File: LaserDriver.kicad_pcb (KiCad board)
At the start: 2 copper layers, 21 parts, among them J100 Screw_Terminal_01x02, J101 Screw_Terminal_01x02, J102 Screw_Terminal_01x02, U1 TPS92513DGQR

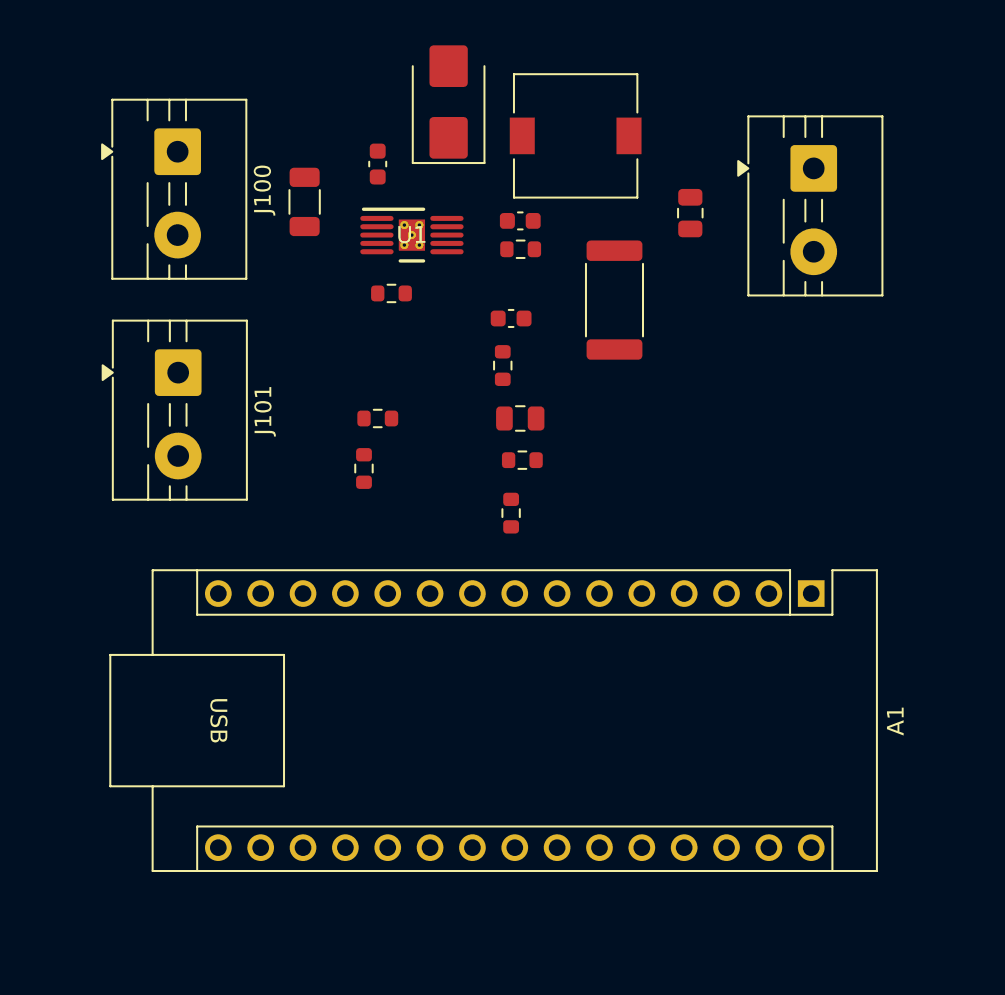
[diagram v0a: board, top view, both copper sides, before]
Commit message: add arduino 3d model
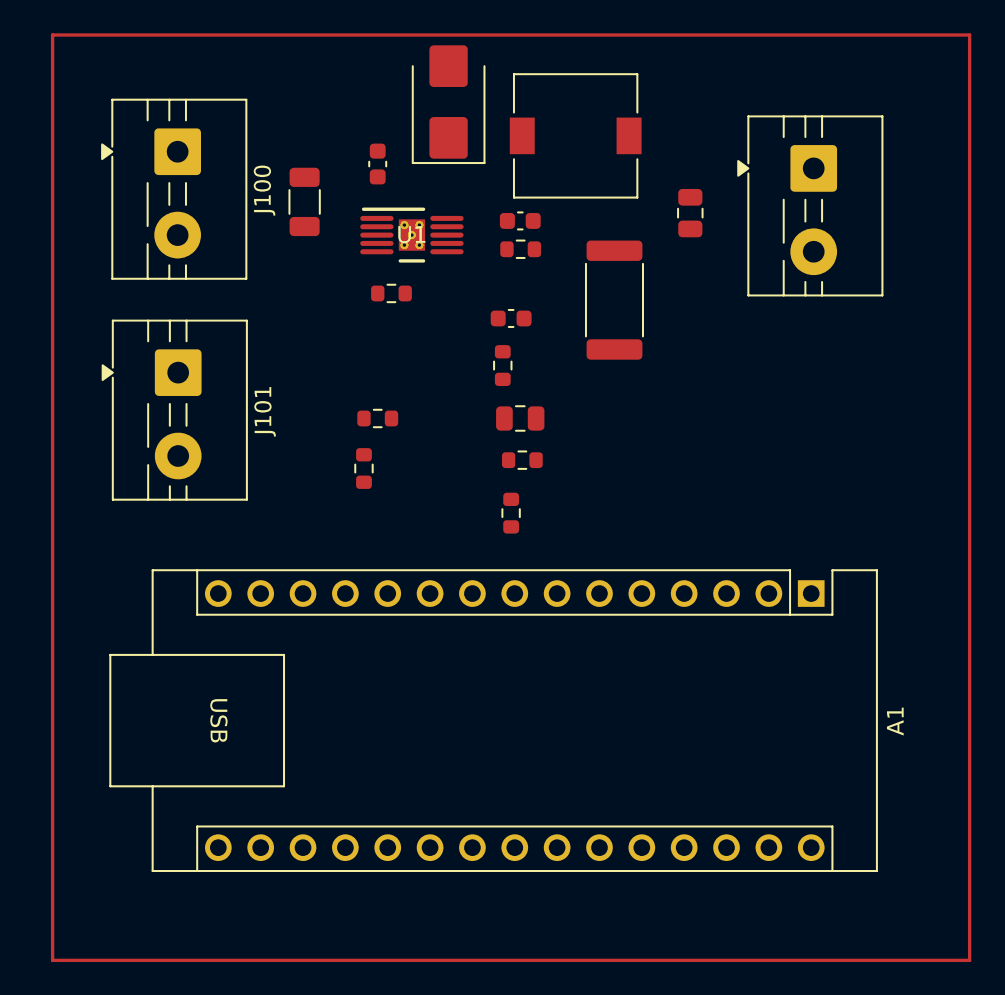
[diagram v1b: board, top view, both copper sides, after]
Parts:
- A1: footprint Module:Arduino_Nano -> Arduino:Arduino_Nano
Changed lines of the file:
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@@
 		)
 	)
-	(footprint "Module:Arduino_Nano"
+	(footprint "Arduino:Arduino_Nano"
 		(layer "F.Cu")
 		(at 69.5 119.5 -90)
@@
 		(tags "Arduino Nano")
 		(property "Reference" "A1"
-			(at 7.62 -5.08 90)
+			(at 7.62 -5.08 270)
 			(layer "F.SilkS")
 			(effects
@@
 			)
 			(scale
+				(xyz 2 1 1)
+			)
+			(rotate
+				(xyz -0 -0 -0)
+			)
+		)
+		(model "${KICAD9_FOOTPRINT_DIR}/Connector_PinSocket_2.54mm.pretty/PinSocket_1x15_P2.54mm_Horizontal.kicad_mod"
+			(offset
+				(xyz 0 0 0)
+			)
+			(scale
+				(xyz 1 1 1)
+			)
+			(rotate
+				(xyz -0 -0 -0)
+			)
+		)
+		(model "${KICAD9_3DMODEL_DIR}/Connector_PinSocket_2.54mm.3dshapes/PinSocket_1x15_P2.54mm_Vertical.step"
+			(offset
+				(xyz 0 0 0)
+			)
+			(scale
 				(xyz 1 1 1)
 			)
@@
 			)
 		)
+		(model "${KICAD9_3DMODEL_DIR}/Connector_PinSocket_2.54mm.3dshapes/PinSocket_1x15_P2.54mm_Vertical.step"
+			(offset
+				(xyz 15.25 0 0)
+			)
+			(scale
+				(xyz 1 1 1)
+			)
+			(rotate
+				(xyz -0 -0 -0)
+			)
+		)
+		(model "/home/gorgalion/Downloads/arduino_nano.x3d"
+			(offset
+				(xyz 0 0 8.5)
+			)
+			(scale
+				(xyz 1 1 1)
+			)
+			(rotate
+				(xyz -0 -0 -0)
+			)
+		)
 	)
 	(footprint "Capacitor_SMD:C_0603_1608Metric"
@@
 		)
 	)
+	(gr_rect
+		(start 24 86)
+		(end 79 141.5)
+		(stroke
+			(width 0.2)
+			(type default)
+		)
+		(fill no)
+		(layer "F.Cu")
+	)
 	(embedded_fonts no)

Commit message: added esd protection
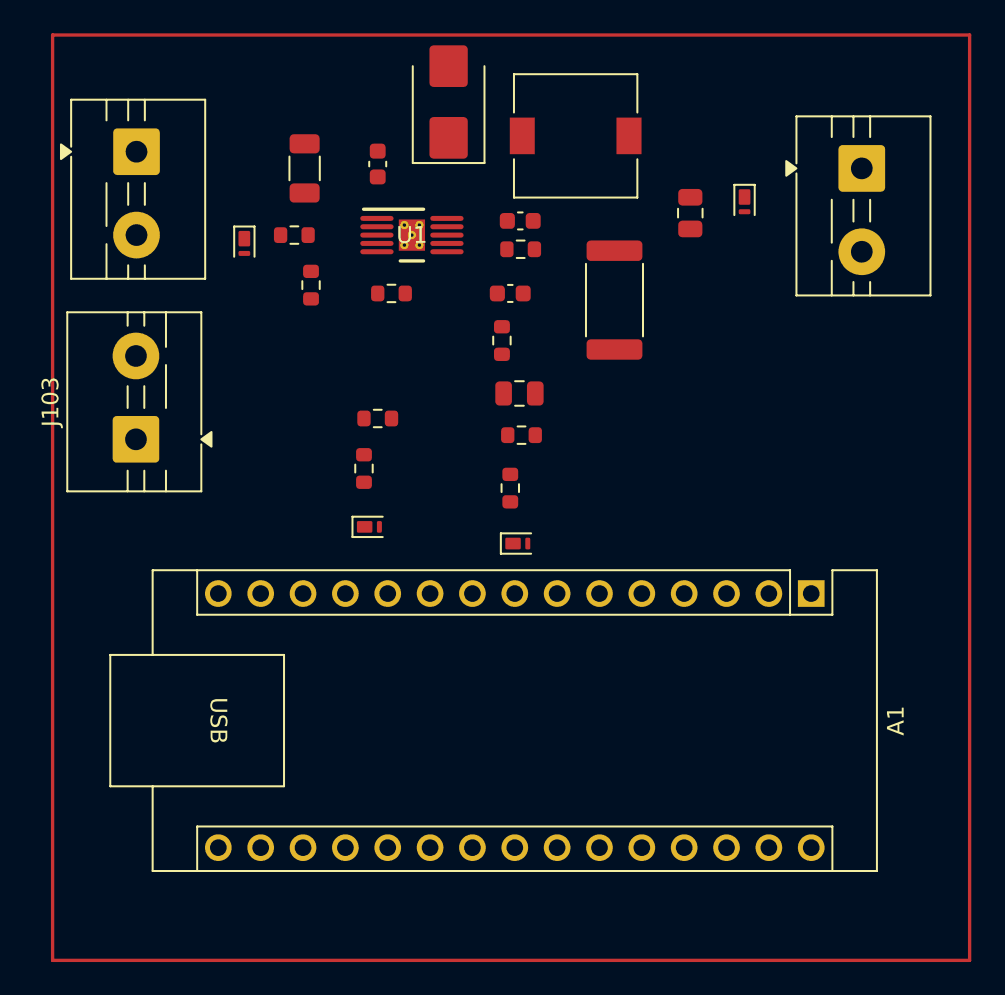
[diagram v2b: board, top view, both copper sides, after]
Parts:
- removed J101: Screw_Terminal_01x02, TerminalBlock:TerminalBlock_MaiXu_MX126-5.0-02P_1x02_P5.00mm
- added D100: PTVS12VZ1USK, Diode_SMD:Nexperia_DSN1608-2_1.6x0.8mm, F.Cu at (35.5, 98.5)
- added D102: PTVS5V0Z1USK, Diode_SMD:Nexperia_DSN1608-2_1.6x0.8mm, F.Cu at (65.5, 96.0)
- added D103: PTVS5V0Z1USK, Diode_SMD:Nexperia_DSN1608-2_1.6x0.8mm, F.Cu at (43.0, 115.5)
- added D104: PTVS5V0Z1USK, Diode_SMD:Nexperia_DSN1608-2_1.6x0.8mm, F.Cu at (51.9, 116.5)
- added J103: Screw_Terminal_01x02, TerminalBlock:TerminalBlock_MaiXu_MX126-5.0-02P_1x02_P5.00mm, F.Cu at (29.0, 110.2)
- added R111: 220k, Resistor_SMD:R_0603_1608Metric, F.Cu at (38.5, 98.0)
- added R112: 30k, Resistor_SMD:R_0603_1608Metric, F.Cu at (39.5, 101.0)
- moved J102 2.88 mm to (72.5, 94.0)
- moved J100 2.47 mm to (29.0, 93.0)
- moved C100 2.01 mm to (39.1, 94.0)
- moved C105 1.50 mm to (51.5, 101.5)
- moved C106 1.50 mm to (52.0, 107.5)
- moved R106 1.50 mm to (51.0, 104.3)
- moved R107 1.50 mm to (51.5, 113.2)
- moved R108 1.50 mm to (52.1, 110.0)
- renumbered D100 to D101
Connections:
- A1 pad 11: /Start -> unconnected-(A1-D8-Pad11)
- A1 pad 12: unconnected-(A1-D9-Pad12) -> Net-(A1-D9)
- A1 pad 14: Net-(A1-D11) -> unconnected-(A1-D11-Pad14)
- J100 pad 1: GND -> Net-(J100-Pin_1)
- R109 pad 2: Net-(A1-D11) -> Net-(A1-D9)

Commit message: power changes
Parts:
- U1: footprint TPS:DGQ0010D_M -> TPS:DGQ0010D_L
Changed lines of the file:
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@@
 	(generator_version "9.0")
 	(general
-		(thickness 1.6)
+		(thickness 1.64)
 		(legacy_teardrops no)
 	)
@@
 	)
 	(setup
+		(stackup
+			(layer "F.SilkS"
+				(type "Top Silk Screen")
+			)
+			(layer "F.Paste"
+				(type "Top Solder Paste")
+			)
+			(layer "F.Mask"
+				(type "Top Solder Mask")
+				(thickness 0.01)
+			)
+			(layer "F.Cu"
+				(type "copper")
+				(thickness 0.035)
+			)
+			(layer "dielectric 1"
+				(type "core")
+				(thickness 1.55)
+				(material "FR4")
+				(epsilon_r 4.5)
+				(loss_tangent 0.02)
+			)
+			(layer "B.Cu"
+				(type "copper")
+				(thickness 0.035)
+			)
+			(layer "B.Mask"
+				(type "Bottom Solder Mask")
+				(thickness 0.01)
+			)
+			(layer "B.Paste"
+				(type "Bottom Solder Paste")
+			)
+			(layer "B.SilkS"
+				(type "Bottom Silk Screen")
+			)
+			(copper_finish "ENIG")
+			(dielectric_constraints no)
+		)
 		(pad_to_mask_clearance 0)
 		(allow_soldermask_bridges_in_footprints no)
@@
 		)
 	)
-	(footprint "TPS:DGQ0010D_M"
+	(footprint "TPS:DGQ0010D_L"
 		(layer "F.Cu")
 		(at 45.550001 98.000001)
@@
 		)
 		(property "Value" "TPS92513DGQR"
-			(at -2.878001 -8.084001 0)
+			(at 0 0 0)
 			(unlocked yes)
 			(layer "F.Fab")
-			(hide yes)
 			(effects
 				(font
@@
 		(attr smd)
 		(fp_line
-			(start -2.899999 -1.549999)
-			(end 0.700001 -1.549999)
+			(start -2.6 -1.549999)
+			(end 0.900001 -1.549999)
 			(stroke
 				(width 0.2)
@@
 		)
 		(fp_line
-			(start -0.699999 1.549999)
-			(end 0.700001 1.549999)
+			(start -0.900001 1.549999)
+			(end 0.900001 1.549999)
 			(stroke
 				(width 0.2)
@@
 		)
 		(fp_line
-			(start -3.599998 -2.050001)
-			(end 3.6 -2.050001)
+			(start -2.849999 -1.650002)
+			(end 2.849999 -1.650002)
 			(stroke
 				(width 0.05)
@@
 		)
 		(fp_line
-			(start -3.599998 2.049998)
-			(end -3.599998 -2.050001)
+			(start -2.849999 1.649999)
+			(end -2.849999 -1.650002)
 			(stroke
 				(width 0.05)
@@
 		)
 		(fp_line
-			(start -3.599998 2.049998)
-			(end 3.6 2.049998)
+			(start -2.849999 1.649999)
+			(end 2.849999 1.649999)
 			(stroke
 				(width 0.05)
@@
 		(fp_line
 			(start -0.499999 0)
-			(end 0.500002 0)
+			(end 0.499999 0)
 			(stroke
 				(width 0.1)
@@
 		)
 		(fp_line
-			(start 0.000003 0.499999)
-			(end 0.000003 -0.500002)
+			(start 0 0.499999)
+			(end 0 -0.500002)
 			(stroke
 				(width 0.1)
@@
 		)
 		(fp_line
-			(start 3.6 2.049998)
-			(end 3.6 -2.050001)
+			(start 2.849999 1.649999)
+			(end 2.849999 -1.650002)
 			(stroke
 				(width 0.05)
@@
 			(layer "F.Fab")
 		)
+		(fp_text user "Designator9"
+			(at -2.6924 -2.6924 0)
+			(unlocked yes)
+			(layer "F.SilkS")
+			(effects
+				(font
+					(size 1 1)
+					(thickness 0.15)
+				)
+			)
+		)
 		(fp_text user "${REFERENCE}"
 			(at 0 0 0)
@@
 		)
 		(pad "1" smd oval
-			(at -2.099998 -1.000001 90)
-			(size 0.299999 2.000001)
+			(at -2.025 -1.000001 90)
+			(size 0.249999 1.45)
 			(layers "F.Cu" "F.Mask" "F.Paste")
 			(net 33 "Net-(U1-BOOT)")
@@
 		)
 		(pad "2" smd oval
-			(at -2.099998 -0.500002 90)
-			(size 0.299999 2.000001)
+			(at -2.025 -0.500002 90)
+			(size 0.249999 1.45)
 			(layers "F.Cu" "F.Mask" "F.Paste")
 			(net 32 "Net-(D100-K)")
@@
 		)
 		(pad "3" smd oval
-			(at -2.099998 0 90)
-			(size 0.299999 2.000001)
+			(at -2.025 0 90)
+			(size 0.249999 1.45)
 			(layers "F.Cu" "F.Mask" "F.Paste")
 			(net 42 "Net-(U1-UVLO)")
@@
 		)
 		(pad "4" smd oval
-			(at -2.099998 0.499999 90)
-			(size 0.299999 2.000001)
+			(at -2.025 0.499999 90)
+			(size 0.249999 1.45)
 			(layers "F.Cu" "F.Mask" "F.Paste")
 			(net 41 "/PWM")
@@
 		)
 		(pad "5" smd oval
-			(at -2.099998 1.000001 90)
-			(size 0.299999 2.000001)
+			(at -2.025 1.000001 90)
+			(size 0.249999 1.45)
 			(layers "F.Cu" "F.Mask" "F.Paste")
 			(net 39 "Net-(U1-RT_CLK)")
@@
 		)
 		(pad "6" smd oval
-			(at 2.100001 1.000001 90)
-			(size 0.299999 2.000001)
+			(at 2.025 1.000001 90)
+			(size 0.249999 1.45)
 			(layers "F.Cu" "F.Mask" "F.Paste")
 			(net 36 "/DAC")
@@
 		)
 		(pad "7" smd oval
-			(at 2.100001 0.499999 90)
-			(size 0.299999 2.000001)
+			(at 2.025 0.499999 90)
+			(size 0.249999 1.45)
 			(layers "F.Cu" "F.Mask" "F.Paste")
 			(net 40 "Net-(U1-ISENSE)")
@@
 		)
 		(pad "8" smd oval
-			(at 2.100001 0 90)
-			(size 0.299999 2.000001)
+			(at 2.025 0 90)
+			(size 0.249999 1.45)
 			(layers "F.Cu" "F.Mask" "F.Paste")
 			(net 31 "Net-(U1-COMP)")
@@
 		)
 		(pad "9" smd oval
-			(at 2.100001 -0.500002 90)
-			(size 0.299999 2.000001)
+			(at 2.025 -0.500002 90)
+			(size 0.249999 1.45)
 			(layers "F.Cu" "F.Mask" "F.Paste")
 			(net 2 "GND")
@@
 		)
 		(pad "10" smd oval
-			(at 2.100001 -1.000001 90)
-			(size 0.299999 2.000001)
+			(at 2.025 -1.000001 90)
+			(size 0.249999 1.45)
 			(layers "F.Cu" "F.Mask" "F.Paste")
 			(net 30 "Net-(D101-K)")
@@
 		)
 		(embedded_fonts no)
+		(model "/home/gorgalion/Downloads/TPS92513DGQT.STEP"
+			(offset
+				(xyz 0 0 0)
+			)
+			(scale
+				(xyz 1 1 1)
+			)
+			(rotate
+				(xyz -90 -0 -0)
+			)
+		)
 	)
 	(footprint "Resistor_SMD:R_0603_1608Metric"

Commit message: compactified design
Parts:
- removed J103: Screw_Terminal_01x02, TerminalBlock:TerminalBlock_MaiXu_MX126-5.0-02P_1x02_P5.00mm
- J100: value Screw_Terminal_01x02 -> Screw_Terminal_01x04; footprint TerminalBlock:TerminalBlock_MaiXu_MX126-5.0-02P_1x02_P5.00mm -> TerminalBlock:TerminalBlock_MaiXu_MX126-5.0-04P_1x04_P5.00mm
- moved J100 17.7 mm to (31.5, 110.5), turned to 90 degrees
- moved J102 8.54 mm to (67.0, 100.5)
- moved R109 8.29 mm to (40.5, 104.0)
- moved C104 6.44 mm to (61.0, 103.0)
- moved C100 6.23 mm to (42.0, 99.5)
- moved D101 6.03 mm to (48.5, 96.0)
- moved D102 5.38 mm to (61.5, 99.6), turned to 90 degrees
- moved R110 5.10 mm to (42.5, 104.0), turned to -90 degrees
- moved C103 4.86 mm to (44.5, 98.5)
- moved R105 4.65 mm to (57.0, 106.5)
- moved R104 4.50 mm to (52.0, 103.3)
- moved L100 4.49 mm to (56.0, 96.5)
- moved C102 4.35 mm to (52.0, 101.5)
- moved R111 4.29 mm to (37.5, 102.2)
- moved U1 4.22 mm to (46.6, 102.1)
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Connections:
- J100 pad 1: Net-(J100-Pin_1) -> GND
- J100 pad 2: Net-(D100-K) -> Net-(J100-Pin_2)

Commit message: finihsed placing
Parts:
- added H1: MountingHole, MountingHole:MountingHole_3.2mm_M3, F.Cu at (35.0, 128.0)
- added H2: MountingHole, MountingHole:MountingHole_3.2mm_M3, F.Cu at (64.0, 104.0)
- added H3: MountingHole, MountingHole:MountingHole_3.2mm_M3, F.Cu at (64.0, 128.0)
- J100: footprint TerminalBlock:TerminalBlock_MaiXu_MX126-5.0-04P_1x04_P5.00mm -> TerminalBlock:TerminalBlock_Xinya_XY308-2.54-4P_1x04_P2.54mm_Horizontal
- J102: footprint TerminalBlock:TerminalBlock_MaiXu_MX126-5.0-02P_1x02_P5.00mm -> TerminalBlock:TerminalBlock_Xinya_XY308-2.54-2P_1x02_P2.54mm_Horizontal
- moved J102 12.6 mm to (65.0, 113.0)
- moved C104 11.5 mm to (58.5, 114.2)
- moved J100 11.2 mm to (39.8, 103.0), turned to 180 degrees
- moved D102 10.9 mm to (64.6, 110.0), turned to 180 degrees
- moved D100 10.7 mm to (32.3, 107.5), turned to 0 degrees
- moved R108 10.2 mm to (43.2, 115.8), turned to 90 degrees
- moved C100 10.1 mm to (38.1, 108.8), turned to 180 degrees
- moved R106 9.97 mm to (45.0, 115.8)
- moved C106 9.64 mm to (47.0, 116.0), turned to 90 degrees
- moved C103 9.60 mm to (42.0, 107.8), turned to 0 degrees
- moved C105 9.35 mm to (46.0, 113.2)
- moved R111 9.14 mm to (35.0, 111.0)
- moved R104 9.02 mm to (48.4, 111.6)
- moved D101 9.02 mm to (46.1, 104.7)
- moved C102 9.01 mm to (48.6, 109.8)
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- renumbered U1 to U100
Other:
- board outline added: 39 x 38 mm

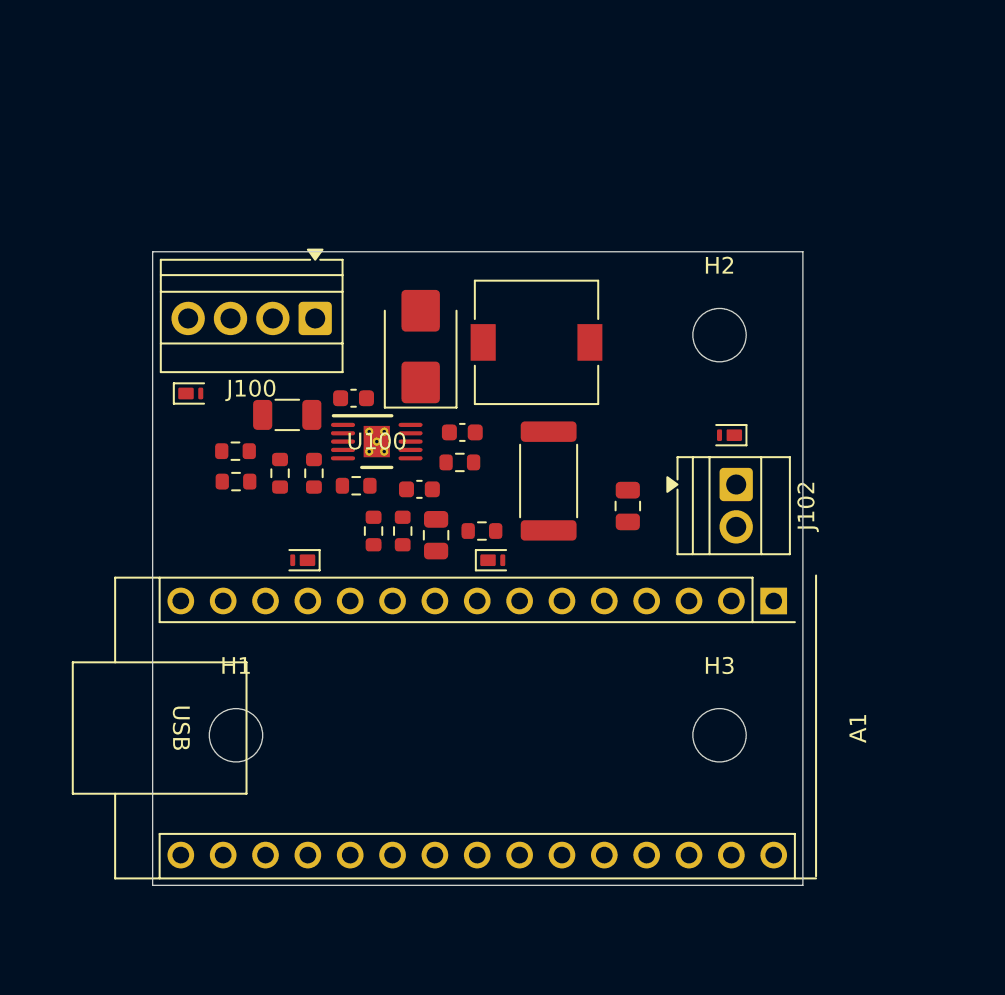
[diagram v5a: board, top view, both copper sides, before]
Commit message: corrected arduino footprint
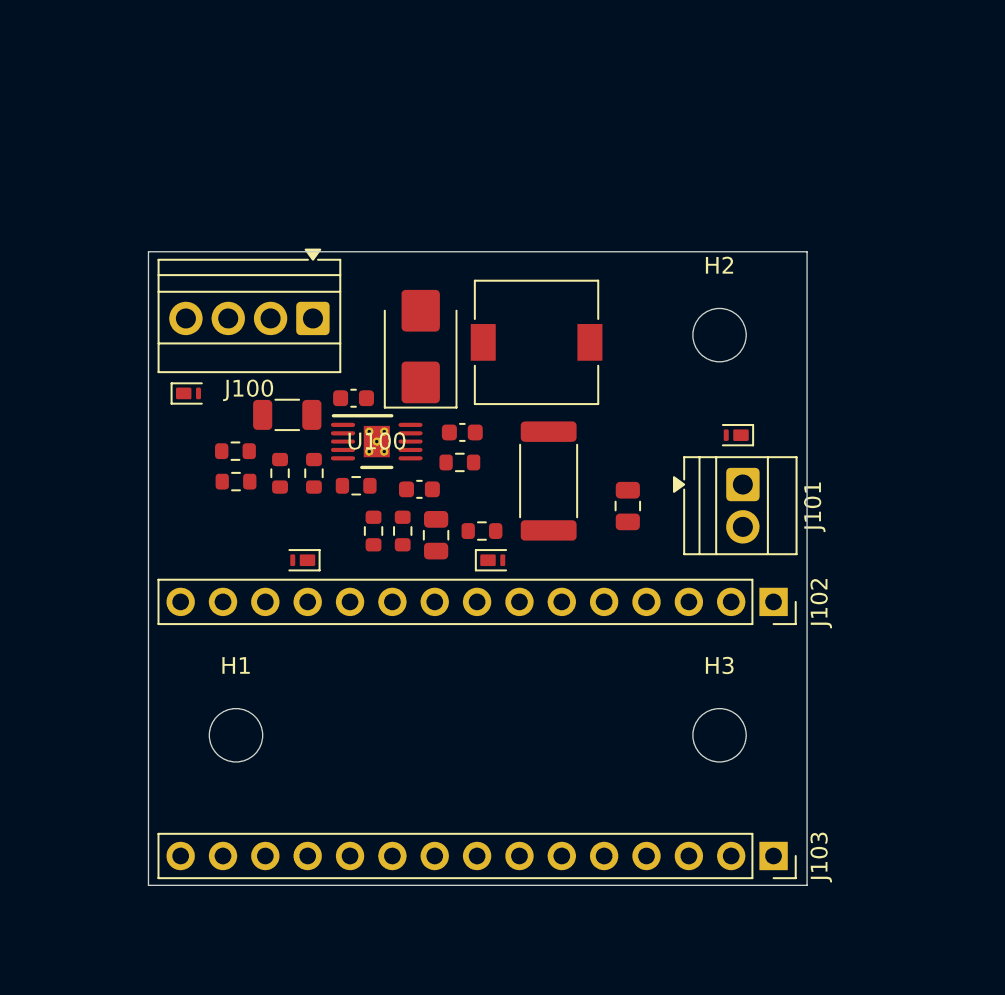
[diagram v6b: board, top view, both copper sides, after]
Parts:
- removed A1: Arduino_Nano_v3.x, Arduino:Arduino_Nano
- added J102: nano_left, Connector_PinSocket_2.54mm:PinSocket_1x15_P2.54mm_Vertical, F.Cu at (67.2, 120.0)
- added J103: nano_right, Connector_PinSocket_2.54mm:PinSocket_1x15_P2.54mm_Vertical, F.Cu at (67.2, 135.2)
- moved D102 0.40 mm to (65.0, 110.0)
- moved J101 0.40 mm to (65.4, 113.0)
- moved D100 0.13 mm to (32.1, 107.5)
- moved J100 0.13 mm to (39.6, 103.0)
- renumbered J102 to J101
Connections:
- net Net-(A1-D5) renamed /ard_DAC
- net Net-(A1-D9) renamed /ard_PWM
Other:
- board size 39 x 38 mm -> 39.5 x 38 mm

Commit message: Routing complete
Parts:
- moved D100 1.87 mm to (31.5, 105.8), turned to 180 degrees
- moved J100 1.75 mm to (39.5, 101.2)
- moved H2 1.75 mm to (64.0, 102.2)
- moved C100 1.58 mm to (39.0, 107.5), turned to 90 degrees
- moved C102 0.69 mm to (49.2, 110.0)
- moved R111 0.53 mm to (35.0, 110.4)
- moved R112 0.53 mm to (35.0, 112.2)
- moved D103 0.25 mm to (39.0, 117.2), turned to 0 degrees
- moved D104 0.25 mm to (50.4, 117.2)
- moved R107 0.25 mm to (49.8, 115.5)
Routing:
- net GND: track 0.00 -> 34.7 mm, vias 0 -> 15
- net Net-(D102-K): track 0.00 -> 21.7 mm
- net Net-(D100-K): track 0.00 -> 21.6 mm
- net Net-(J101-Pin_2): track 0.00 -> 18.2 mm
- net Net-(D101-K): track 0.00 -> 11.2 mm
- net /ard_PWM: track 0.00 -> 7.58 mm
- net Net-(U100-UVLO): track 0.00 -> 7.49 mm
- net Net-(C106-Pad1): track 0.00 -> 6.43 mm
- net /ard_DAC: track 0.00 -> 4.96 mm
- net /PWM: track 0.00 -> 4.01 mm
- net /DAC: track 0.00 -> 3.73 mm
- net Net-(U100-COMP): track 0.00 -> 3.17 mm
- net Net-(U100-ISENSE): track 0.00 -> 2.44 mm
- net Net-(U100-RT_CLK): track 0.00 -> 1.66 mm
- net Net-(U100-BOOT): track 0.00 -> 1.66 mm
- added copper zone on B.Cu, net GND
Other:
- board size 39.5 x 38 mm -> 39.5 x 40 mm
